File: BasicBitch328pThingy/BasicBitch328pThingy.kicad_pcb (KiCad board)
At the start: 2 copper layers, 88.9 x 104.1 mm, 71 parts, among them IC1 LM2597MX-5.0_NOPB, J1 Conn_01x03, J2 Conn_01x03, J3 Conn_02x03_Odd_Even, J4 Conn_01x08, P1 Screw_Terminal_01x02, Q1 2N7000, Q10 IRF9Z34NPBF, Q2 2N7000, Q3 IRF9Z34NPBF, Q4 2N7000, Q5 2N7000, Q6 2N7000, Q7 IRF9Z34NPBF, Q8 IRF9Z34NPBF, Q9 2N7000, U1 ATmega328-P, U2 178.6165.0001, U3 LTV-817, U4 LTV-817, U5 LTV-817, Y1 Crystal

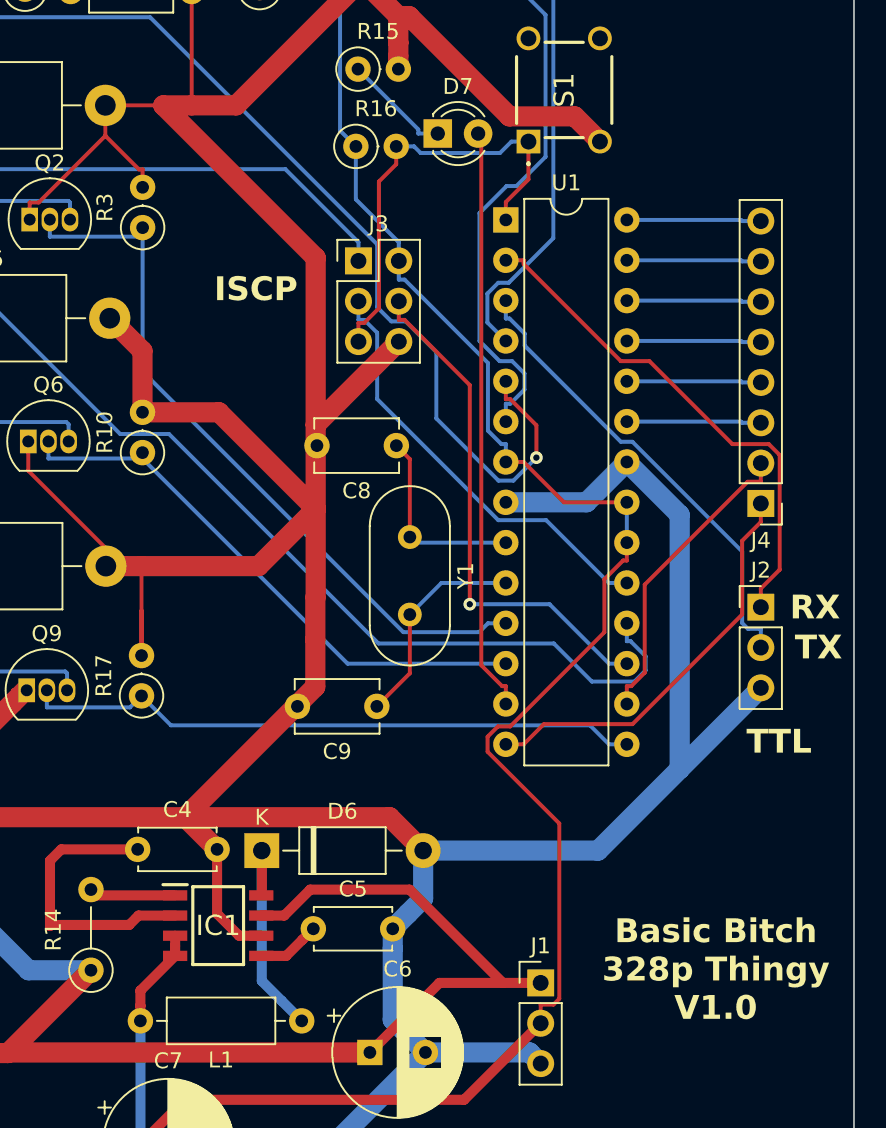
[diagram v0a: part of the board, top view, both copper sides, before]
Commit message: V1.0.1
* Fixed a trace issue
* updated Fab Files
* added bom/ibom.html
* added some code
** BasicFrameWork.ino
** Test.ino
** HeadLightWarningAndEGR.ino
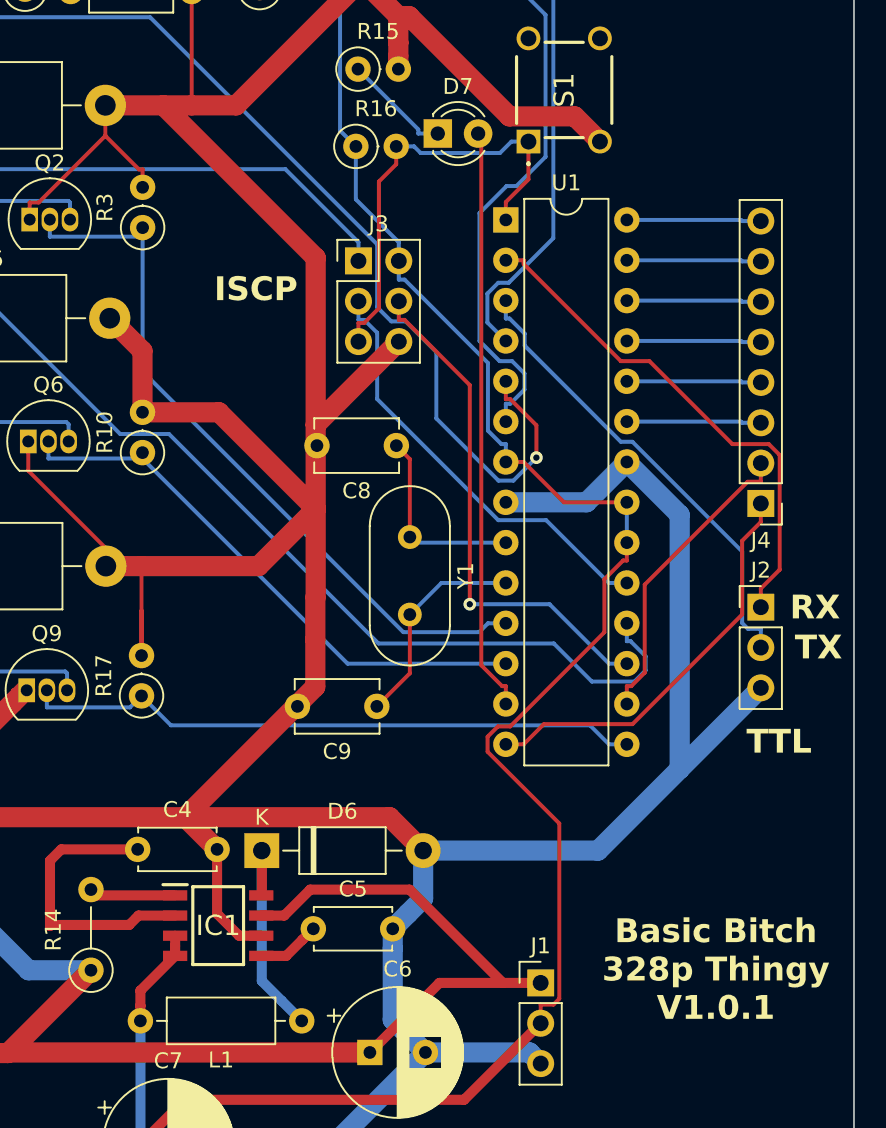
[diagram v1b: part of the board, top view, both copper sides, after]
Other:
- board text added: "Basic Bitch 328p Thingy V1.0.1"
- board text removed: "Basic Bitch 328p Thingy V1.0"
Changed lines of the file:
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@@
       (outputformat 1)
       (mirror false)
-      (drillshape 1)
+      (drillshape 0)
       (scaleselection 1)
-      (outputdirectory "")
+      (outputdirectory "../Fab Files/")
     )
   )
@@
     (effects (font (size 1.5 1.5) (thickness 0.3) bold) (justify left bottom))
   )
-  (gr_text "Basic Bitch \n328p Thingy \nV1.0" (at 171.175468 133.08909) (layer "F.SilkS")
+  (gr_text "Basic Bitch \n328p Thingy \nV1.0.1" (at 171.175468 133.08909) (layer "F.SilkS")
     (effects (font (size 1.5 1.5) (thickness 0.3) bold))
   )
@@
   (segment (start 119.0693 70.3041) (end 119.9137 69.4597) (width 0.25) (layer "F.Cu") (net 2))
   (segment (start 132.595 60.8282) (end 135.916 60.8282) (width 1.27) (layer "F.Cu") (net 2))
+  (segment (start 136.38 78.6769) (end 132.7333 78.6769) (width 1.27) (layer "F.Cu") (net 2))
   (segment (start 108.111 62.7444) (end 108.111 62.8232) (width 1.27) (layer "F.Cu") (net 2))
   (segment (start 132.733 78.6769) (end 132.733 80.5952) (width 0.25) (layer "F.Cu") (net 2))
@@
   (segment (start 132.646 62.4632) (end 132.646 60.8792) (width 1.27) (layer "F.Cu") (net 2))
   (segment (start 135.01 110.507) (end 135.0099 110.5071) (width 0.25) (layer "F.Cu") (net 2))
-  (segment (start 136.38 78.6769) (end 132.7333 78.6769) (width 0.25) (layer "F.Cu") (net 2))
   (segment (start 146.6378 62.4632) (end 146.6378 60.5218) (width 0.25) (layer "B.Cu") (net 2))
   (segment (start 159.443 138.315) (end 160.144 139.016) (width 1.27) (layer "B.Cu") (net 2))

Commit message: revamping this to have a CANBus Interface and swaping things to a SMD to save Space.
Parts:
- removed J3: Conn_02x03_Odd_Even, Connector_PinHeader_2.54mm:PinHeader_2x03_P2.54mm_Vertical
- removed J4: Conn_01x08, Connector_PinHeader_2.54mm:PinHeader_1x08_P2.54mm_Vertical
- added C10: 220nF, Capacitor_SMD:C_1206_3216Metric_Pad1.33x1.80mm_HandSolder, F.Cu at (226.4, 81.3)
- added C11: 22pf, Capacitor_SMD:C_1206_3216Metric_Pad1.33x1.80mm_HandSolder, F.Cu at (206.9, 66.8)
- added C12: 22pf, Capacitor_SMD:C_1206_3216Metric_Pad1.33x1.80mm_HandSolder, F.Cu at (206.9, 70.1)
- added C13: 100nf, Capacitor_SMD:C_1206_3216Metric_Pad1.33x1.80mm_HandSolder, F.Cu at (206.9, 73.5)
- added C14: 100nf, Capacitor_SMD:C_1206_3216Metric_Pad1.33x1.80mm_HandSolder, F.Cu at (206.9, 76.8)
- added D9: PESD5V0L2UU,115, SamacSys_Parts:SOT65P210X110-3N, F.Cu at (212.2, 95.4)
- added P2: Screw_Terminal_01x02, TerminalBlock_Phoenix:TerminalBlock_Phoenix_MKDS-1,5-2-5.08_1x02_P5.08mm_Horizontal, F.Cu at (228.4, 71.3)
- added R26: 10k, Resistor_SMD:R_1206_3216Metric_Pad1.30x1.75mm_HandSolder, F.Cu at (206.9, 80.1)
- added R27: 17k, Resistor_SMD:R_1206_3216Metric_Pad1.30x1.75mm_HandSolder, F.Cu at (205.9, 89.0)
- added R28: 120, Resistor_SMD:R_1206_3216Metric_Pad1.30x1.75mm_HandSolder, F.Cu at (205.9, 93.0)
- added U6: MCP2515-xSO, Package_SO:SOIC-18W_7.5x11.6mm_P1.27mm, F.Cu at (216.3, 71.8)
- added U7: MCP2551-I-SN, Package_SO:SOIC-8_3.9x4.9mm_P1.27mm, F.Cu at (214.2, 90.3)
- added Y2: 16MHz, Crystal:Crystal_HC49-U_Vertical, F.Cu at (213.9, 81.6)
- C1, C3: value 220nF -> 0.1uF; footprint Capacitor_THT:C_Disc_D5.1mm_W3.2mm_P5.00mm -> Capacitor_THT:C_Disc_D4.7mm_W2.5mm_P5.00mm
- C2: value 220nF -> 100nf; footprint Capacitor_THT:C_Disc_D5.1mm_W3.2mm_P5.00mm -> Capacitor_SMD:C_1206_3216Metric_Pad1.33x1.80mm_HandSolder
- C4: value 0.1uF -> 68uF; footprint Capacitor_THT:C_Disc_D4.7mm_W2.5mm_P5.00mm -> Capacitor_THT:CP_Radial_D8.0mm_P3.50mm
- C5: value 0.1uF -> 22pF; footprint Capacitor_THT:C_Disc_D4.7mm_W2.5mm_P5.00mm -> Capacitor_SMD:C_1206_3216Metric_Pad1.33x1.80mm_HandSolder
- C6: value 68uF -> 120uF
- C7: value 120uF -> 22pF; footprint Capacitor_THT:CP_Radial_D8.0mm_P3.50mm -> Capacitor_SMD:C_1206_3216Metric_Pad1.33x1.80mm_HandSolder
- C8, C9: footprint Capacitor_THT:C_Disc_D5.1mm_W3.2mm_P5.00mm -> Capacitor_SMD:C_1206_3216Metric_Pad1.33x1.80mm_HandSolder
- D1: value 1N4007 -> LED; footprint Diode_THT:D_DO-41_SOD81_P10.16mm_Horizontal -> LED_THT:LED_D3.0mm
- D2: value STPS3150RL -> 1N5817; footprint Diode_THT:D_DO-201_P15.24mm_Horizontal -> Diode_THT:D_DO-41_SOD81_P10.16mm_Horizontal
- D4: value 1N4007 -> STPS3150RL; footprint Diode_THT:D_DO-41_SOD81_P10.16mm_Horizontal -> Diode_THT:D_DO-201_P15.24mm_Horizontal
- D5: value STPS3150RL -> 1N4007; footprint Diode_THT:D_DO-201_P15.24mm_Horizontal -> Diode_THT:D_DO-41_SOD81_P10.16mm_Horizontal
- D6: value 1N5817 -> 1N4007
- D7: value LED -> STPS3150RL; footprint LED_THT:LED_D3.0mm -> Diode_THT:D_DO-201_P15.24mm_Horizontal
- J1: value Conn_01x03 -> TTL_Programmer; footprint Connector_PinHeader_2.54mm:PinHeader_1x03_P2.54mm_Vertical -> Connector_PinHeader_2.54mm:PinHeader_1x06_P2.54mm_Vertical
- J2: value Conn_01x03 -> Conn_01x02; footprint Connector_PinHeader_2.54mm:PinHeader_1x03_P2.54mm_Vertical -> Connector_PinHeader_2.54mm:PinHeader_1x02_P2.54mm_Vertical
- Q1, Q4: value 2N7000 -> IRF9Z34NPBF; footprint Package_TO_SOT_THT:TO-92_Inline -> SamacSys_Parts:TO254P469X1042X1967-3P
- Q3, Q7: value IRF9Z34NPBF -> 2N7000; footprint SamacSys_Parts:TO254P469X1042X1967-3P -> Package_TO_SOT_THT:TO-92_Inline
- R1: value 470 -> 10k; footprint Resistor_THT:R_Axial_DIN0207_L6.3mm_D2.5mm_P2.54mm_Vertical -> Resistor_SMD:R_1206_3216Metric_Pad1.30x1.75mm_HandSolder
- R10: value 1M -> 100k; footprint Resistor_THT:R_Axial_DIN0207_L6.3mm_D2.5mm_P2.54mm_Vertical -> Resistor_SMD:R_1206_3216Metric_Pad1.30x1.75mm_HandSolder
- R11, R4: value 100k -> 10k; footprint Resistor_THT:R_Axial_DIN0207_L6.3mm_D2.5mm_P2.54mm_Vertical -> Resistor_SMD:R_1206_3216Metric_Pad1.30x1.75mm_HandSolder
- R12, R5: value 10k -> 470; footprint Resistor_THT:R_Axial_DIN0207_L6.3mm_D2.5mm_P2.54mm_Vertical -> Resistor_SMD:R_1206_3216Metric_Pad1.30x1.75mm_HandSolder
- R13, R19: value 10k -> 5k; footprint Resistor_THT:R_Axial_DIN0207_L6.3mm_D2.5mm_P2.54mm_Vertical -> Resistor_SMD:R_1206_3216Metric_Pad1.30x1.75mm_HandSolder
- R14: value 10k -> 5k; footprint Resistor_THT:R_Axial_DIN0207_L6.3mm_D2.5mm_P5.08mm_Vertical -> Resistor_SMD:R_1206_3216Metric_Pad1.30x1.75mm_HandSolder
- R15: value 330 -> 5k; footprint Resistor_THT:R_Axial_DIN0207_L6.3mm_D2.5mm_P2.54mm_Vertical -> Resistor_SMD:R_1206_3216Metric_Pad1.30x1.75mm_HandSolder
- R16: value 330 -> 470; footprint Resistor_THT:R_Axial_DIN0207_L6.3mm_D2.5mm_P2.54mm_Vertical -> Resistor_SMD:R_1206_3216Metric_Pad1.30x1.75mm_HandSolder
- R17: value 1M -> 5k; footprint Resistor_THT:R_Axial_DIN0207_L6.3mm_D2.5mm_P2.54mm_Vertical -> Resistor_SMD:R_1206_3216Metric_Pad1.30x1.75mm_HandSolder
- R18: value 100k -> 5k; footprint Resistor_THT:R_Axial_DIN0207_L6.3mm_D2.5mm_P2.54mm_Vertical -> Resistor_SMD:R_1206_3216Metric_Pad1.30x1.75mm_HandSolder
- R2: value 5k -> 330; footprint Resistor_THT:R_Axial_DIN0207_L6.3mm_D2.5mm_P2.54mm_Vertical -> Resistor_SMD:R_1206_3216Metric_Pad1.30x1.75mm_HandSolder
- R20, R23, R9: value 5k -> 1M; footprint Resistor_THT:R_Axial_DIN0207_L6.3mm_D2.5mm_P2.54mm_Vertical -> Resistor_SMD:R_1206_3216Metric_Pad1.30x1.75mm_HandSolder
- R21, R24: value 5k -> 100k; footprint Resistor_THT:R_Axial_DIN0207_L6.3mm_D2.5mm_P2.54mm_Vertical -> Resistor_SMD:R_1206_3216Metric_Pad1.30x1.75mm_HandSolder
- R22, R25: value 5k -> 10k; footprint Resistor_THT:R_Axial_DIN0207_L6.3mm_D2.5mm_P2.54mm_Vertical -> Resistor_SMD:R_1206_3216Metric_Pad1.30x1.75mm_HandSolder
- R3: value 1M -> 330; footprint Resistor_THT:R_Axial_DIN0207_L6.3mm_D2.5mm_P2.54mm_Vertical -> Resistor_SMD:R_1206_3216Metric_Pad1.30x1.75mm_HandSolder
- R6, R8: value 470 -> 5k; footprint Resistor_THT:R_Axial_DIN0207_L6.3mm_D2.5mm_P2.54mm_Vertical -> Resistor_SMD:R_1206_3216Metric_Pad1.30x1.75mm_HandSolder
- R7: footprint Resistor_THT:R_Axial_DIN0207_L6.3mm_D2.5mm_P2.54mm_Vertical -> Resistor_SMD:R_1206_3216Metric_Pad1.30x1.75mm_HandSolder
- U1: value ATmega328-P -> 178.6165.0001; footprint Package_DIP:DIP-28_W7.62mm -> SamacSys_Parts:17861650001
- U2: value 178.6165.0001 -> ATmega328-P; footprint SamacSys_Parts:17861650001 -> Package_DIP:DIP-28_W7.62mm
- Z1, Z2: value BZX79C10 -> Screw_Terminal_01x03; footprint SamacSys_Parts:DIOAD1068W53L380D172 -> TerminalBlock_Phoenix:TerminalBlock_Phoenix_MKDS-1,5-3-5.08_1x03_P5.08mm_Horizontal
- Z4, Z5: value Screw_Terminal_01x03 -> BZX79C10; footprint TerminalBlock_Phoenix:TerminalBlock_Phoenix_MKDS-1,5-3-5.08_1x03_P5.08mm_Horizontal -> SamacSys_Parts:DIOAD1068W53L380D172
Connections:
- C1 pad 1: /Input/Input -> Net-(IC1-DELAY)
- C2 pad 1: /Input1/Input -> Net-(J1-Pin_6)
- C2 pad 2: GND -> /RESET
- C3 pad 1: /Input2/Input -> Net-(IC1-~{SHUTDOWN}/SOFT-START)
- C4 pad 1: Net-(IC1-DELAY) -> +VDC
- C5 pad 1: Net-(IC1-~{SHUTDOWN}/SOFT-START) -> Net-(U2-XTAL1/PB6)
- C6 pad 1: +VDC -> +5V
- C7 pad 1: +5V -> Net-(U2-XTAL2/PB7)
- C8 pad 1: Net-(U1-XTAL1/PB6) -> /Input/Input
- C9 pad 1: Net-(U1-XTAL2/PB7) -> /Input1/Input
- D1 pad 1: /Input/Input -> Net-(D1-K)
- D1 pad 2: Net-(D1-A) -> LED
- D2 pad 1: /Output/Output -> Net-(D2-K)
- D3 pad 1: /Input1/Input -> /Input/Input
- D4 pad 1: /Input2/Input -> /Output/Output
- D4 pad 2: Net-(D4-A) -> GND
- D5 pad 1: /Output1/Output -> /Input1/Input
- D5 pad 2: GND -> Net-(D5-A)
- D6 pad 1: Net-(D6-K) -> /Input2/Input
- D6 pad 2: GND -> Net-(D6-A)
- D7 pad 1: Net-(D7-K) -> /Output1/Output
- D7 pad 2: LED -> GND
- IC1 pad 8: Net-(D6-K) -> Net-(D2-K)
- J1 pad 1: +VDC -> GND
- J1 pad 2: +5V -> unconnected-(J1-Pin_2-Pad2)
- J1 pad 3: GND -> +5V
- J2 pad 1: RXttl -> /CANBUS-MCP2551/CANH
- J2 pad 2: TXttl -> Net-(J2-Pin_2)
- L1 pad 1: Net-(D6-K) -> Net-(D2-K)
- Q1 pad 1: GND -> Net-(Q1-Pad1)
- Q1 pad 2: Net-(D1-A) -> Net-(P1-Pin_1)
- Q1 pad 3: Net-(Q1-D) -> Net-(Q1-Pad3)
- Q2 pad 2: Output1 -> Net-(D3-A)
- Q3 pad 1: Net-(Q3-Pad1) -> GND
- Q3 pad 2: /Output/Output -> Output1
- Q3 pad 3: +VDC -> Net-(Q3-D)
- Q4 pad 1: GND -> Net-(Q4-Pad1)
- Q4 pad 2: Net-(D3-A) -> /Output/Output
- Q4 pad 3: Net-(Q4-D) -> +VDC
- Q5 pad 2: Net-(D4-A) -> Net-(D5-A)
- Q6 pad 2: Output2 -> Net-(D6-A)
- Q7 pad 1: Net-(Q7-Pad1) -> GND
- Q7 pad 2: /Output1/Output -> Output2
- Q7 pad 3: +VDC -> Net-(Q7-D)
- Q8 pad 2: Net-(P1-Pin_1) -> /Output1/Output
- Q8 pad 3: Net-(Q8-Pad3) -> +VDC
- R1 pad 1: /Input/Input -> Net-(Q1-Pad1)
- R1 pad 2: Net-(D1-A) -> GND
- R10 pad 1: Output2 -> +VDC
- R10 pad 2: GND -> Net-(Q4-Pad1)
- R11 pad 1: +VDC -> Net-(Q4-Pad1)
- R11 pad 2: Net-(Q7-Pad1) -> Net-(Q3-D)
- R12 pad 1: Net-(Q7-Pad1) -> /Input1/Input
- R12 pad 2: Net-(Q6-D) -> Net-(D5-A)
- R13 pad 1: Net-(Q8-Pad1) -> Net-(D5-A)
- R14 pad 1: +VDC -> +5V
- R14 pad 2: Net-(IC1-ERROR_FLAG) -> Net-(R14-Pad2)
- R15 pad 1: Net-(D7-K) -> +5V
- R15 pad 2: GND -> Input2
- R16 pad 1: +5V -> /Input2/Input
- R16 pad 2: Reset -> Net-(D6-A)
- R17 pad 1: Output3 -> Net-(D6-A)
- R18 pad 1: +VDC -> +5V
- R18 pad 2: Net-(Q10-Pad1) -> Net-(R18-Pad2)
- R19 pad 1: Net-(Q10-Pad1) -> +5V
- R19 pad 2: Net-(Q9-D) -> Input3
- R2 pad 1: Net-(D1-A) -> +5V
- R2 pad 2: GND -> Reset
- R20 pad 1: +5V -> Output2
- R20 pad 2: Input1 -> GND
- R21 pad 1: +5V -> +VDC
- R21 pad 2: Input2 -> Net-(Q8-Pad1)
- R22 pad 1: +5V -> Net-(Q8-Pad1)
- R22 pad 2: Input3 -> Net-(Q7-D)
- R23 pad 1: +5V -> Output3
- R23 pad 2: Net-(R23-Pad2) -> GND
- R24 pad 1: +5V -> +VDC
- R24 pad 2: Net-(R24-Pad2) -> Net-(Q10-Pad1)
- R25 pad 1: +5V -> Net-(Q10-Pad1)
- R25 pad 2: Net-(R25-Pad2) -> Net-(Q9-D)
- R3 pad 1: Output1 -> Net-(D1-K)
- R4 pad 2: Net-(Q3-Pad1) -> Net-(IC1-ERROR_FLAG)
- R5 pad 1: Net-(Q3-Pad1) -> /Input/Input
- R5 pad 2: Net-(Q2-D) -> Net-(D3-A)
- R6 pad 1: /Input1/Input -> Net-(D3-A)
- R6 pad 2: Net-(D3-A) -> GND
- R7 pad 1: Net-(D3-A) -> +5V
- R7 pad 2: GND -> Net-(R7-Pad2)
- R8 pad 1: /Input2/Input -> +5V
- R8 pad 2: Net-(D4-A) -> Input1
- R9 pad 1: Net-(D4-A) -> Output1
- U1 pad 1: Reset -> +VDC
- U1 pad 2: RXttl -> +VDC
- U1 pad 3: TXttl -> Net-(Q1-Pad3)
- U1 pad 4: Input3 -> Net-(Q1-Pad3)
- U1 pad 5: Input1 -> Net-(Q1-Pad3)
- U1 pad 6: Input2 -> Net-(Q1-Pad3)
- U1 pad 7: +5V -> +VDC
- U1 pad 8: GND -> +VDC
- U2 pad 1: +VDC -> Reset
- U2 pad 2: +VDC -> RXttl
- U2 pad 3: Net-(Q8-Pad3) -> TXttl
- U2 pad 4: Net-(Q8-Pad3) -> Input3
- U2 pad 5: Net-(Q8-Pad3) -> Input1
- U2 pad 6: Net-(Q8-Pad3) -> Input2
- U2 pad 7: +VDC -> +5V
- U2 pad 8: +VDC -> GND
- U3 pad 1: Net-(R23-Pad2) -> Net-(R7-Pad2)
- U3 pad 2: Net-(Q1-D) -> Net-(Q2-D)
- U4 pad 1: Net-(R24-Pad2) -> Net-(R14-Pad2)
- U4 pad 2: Net-(Q4-D) -> Net-(Q5-D)
- U5 pad 1: Net-(R25-Pad2) -> Net-(R18-Pad2)
- U5 pad 2: Net-(Q5-D) -> Net-(Q6-D)
- Y1 pad 1: Net-(U1-XTAL1/PB6) -> Net-(U2-XTAL1/PB6)
- Y1 pad 2: Net-(U1-XTAL2/PB7) -> Net-(U2-XTAL2/PB7)
- Z1 pad 1: +VDC -> /Output/Output
- Z1 pad 2: Net-(Q3-Pad1) -> /Output1/Output
- Z2 pad 1: +VDC -> /Input/Input
- Z2 pad 2: Net-(Q7-Pad1) -> /Input1/Input
- Z3 pad 2: Net-(Q10-Pad1) -> Net-(Q4-Pad1)
- Z4 pad 1: /Input/Input -> +VDC
- Z4 pad 2: /Input1/Input -> Net-(Q8-Pad1)
- Z5 pad 1: /Output/Output -> +VDC
- Z5 pad 2: /Output1/Output -> Net-(Q10-Pad1)
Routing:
- net GND: track 455.6 -> 0.00 mm
- net +5V: track 191.2 -> 0.00 mm
- net +VDC: track 168.3 -> 0.00 mm
- net Input1: track 96.7 -> 0.00 mm, vias 1 -> 0
- net MISO: track 91.0 -> 0.00 mm
- net /Input2/Input: track 56.8 -> 0.00 mm
- net Input2: track 55.7 -> 0.00 mm
- net Input3: track 47.2 -> 0.00 mm
- net Output1: track 45.3 -> 0.00 mm
- net /Input1/Input: track 41.0 -> 0.00 mm
- net Output3: track 38.6 -> 0.00 mm
- net LED: track 35.9 -> 0.00 mm
- net Output2: track 35.2 -> 0.00 mm
- net MOSI: track 32.6 -> 0.00 mm, vias 1 -> 0
- net RXttl: track 31.9 -> 0.00 mm
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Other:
- board size 88.9 x 104.1 mm -> 304.7 x 104.1 mm
- board text added: "Basic Bitch 328p Thingy V2.0.0"
- board text removed: "Basic Bitch 328p Thingy V1.0.1"
